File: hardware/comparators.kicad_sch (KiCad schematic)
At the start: 108 parts, among them SW7 SW_DIP_x03, U41 TLV3502AIDR, U42 TLV3502AIDR, U43 TLV3502AIDR, U44 TLV3502AIDR, U45 TLV3502AIDR, U46 TLV3502AIDR, U47 TLV3502AIDR, U48 TLV3502AIDR, U49 TLV3502AIDR, U50 TLV3502AIDR, U51 TLV3502AIDR, U52 TLV3502AIDR, U53 TXB0108PW, U54 TXB0108PW, U55 TXB0108PW

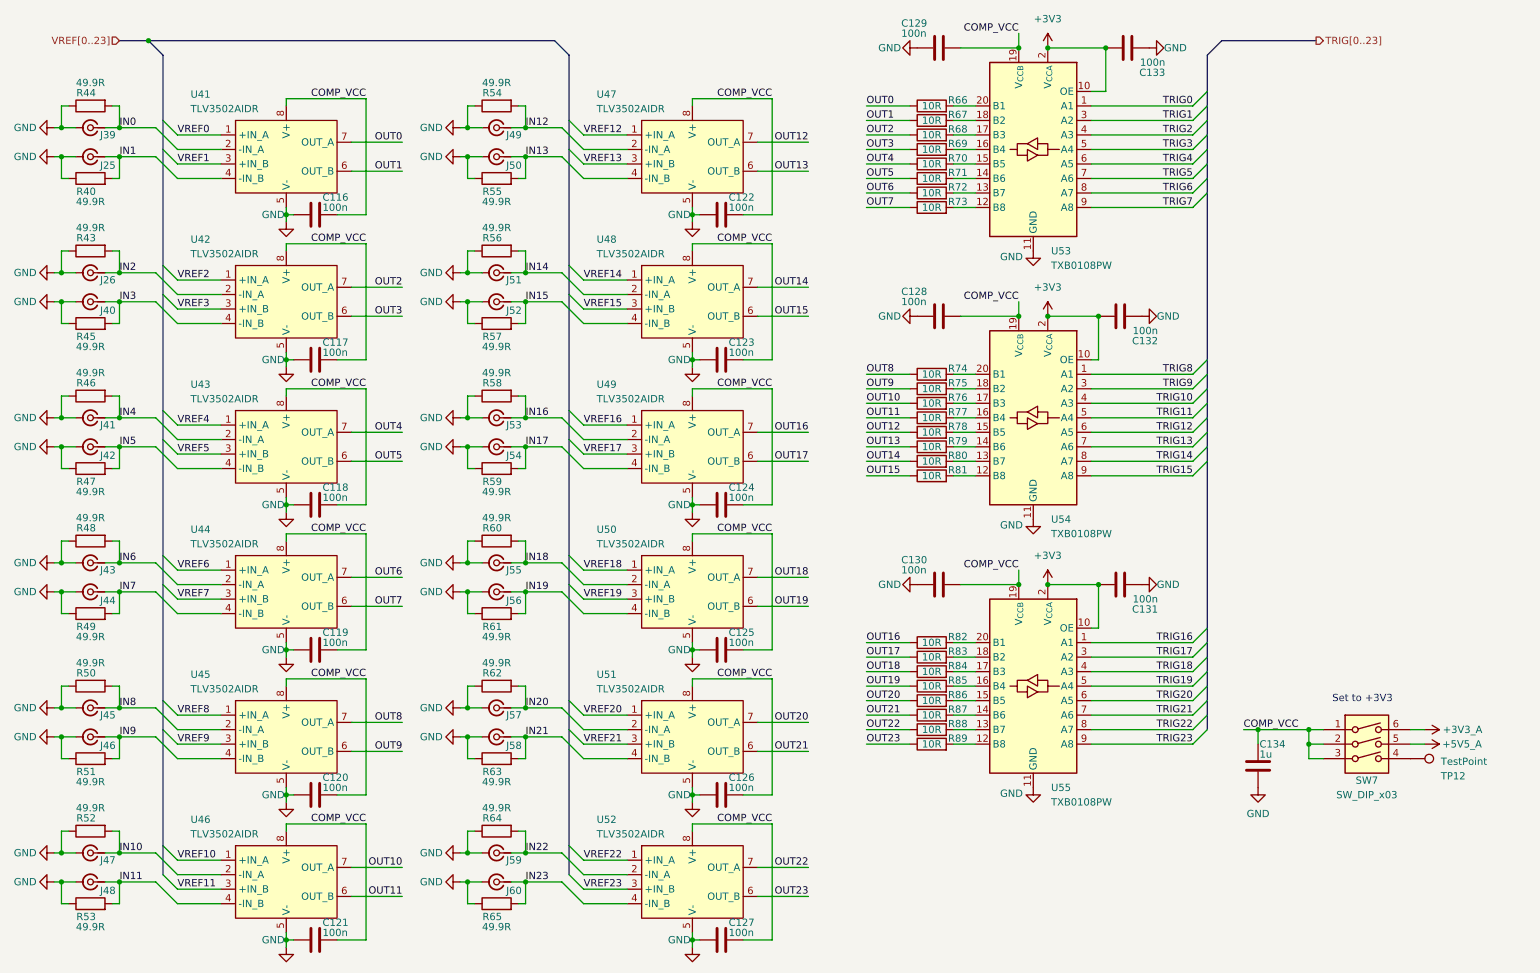
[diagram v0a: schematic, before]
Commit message: complete schematic wiring
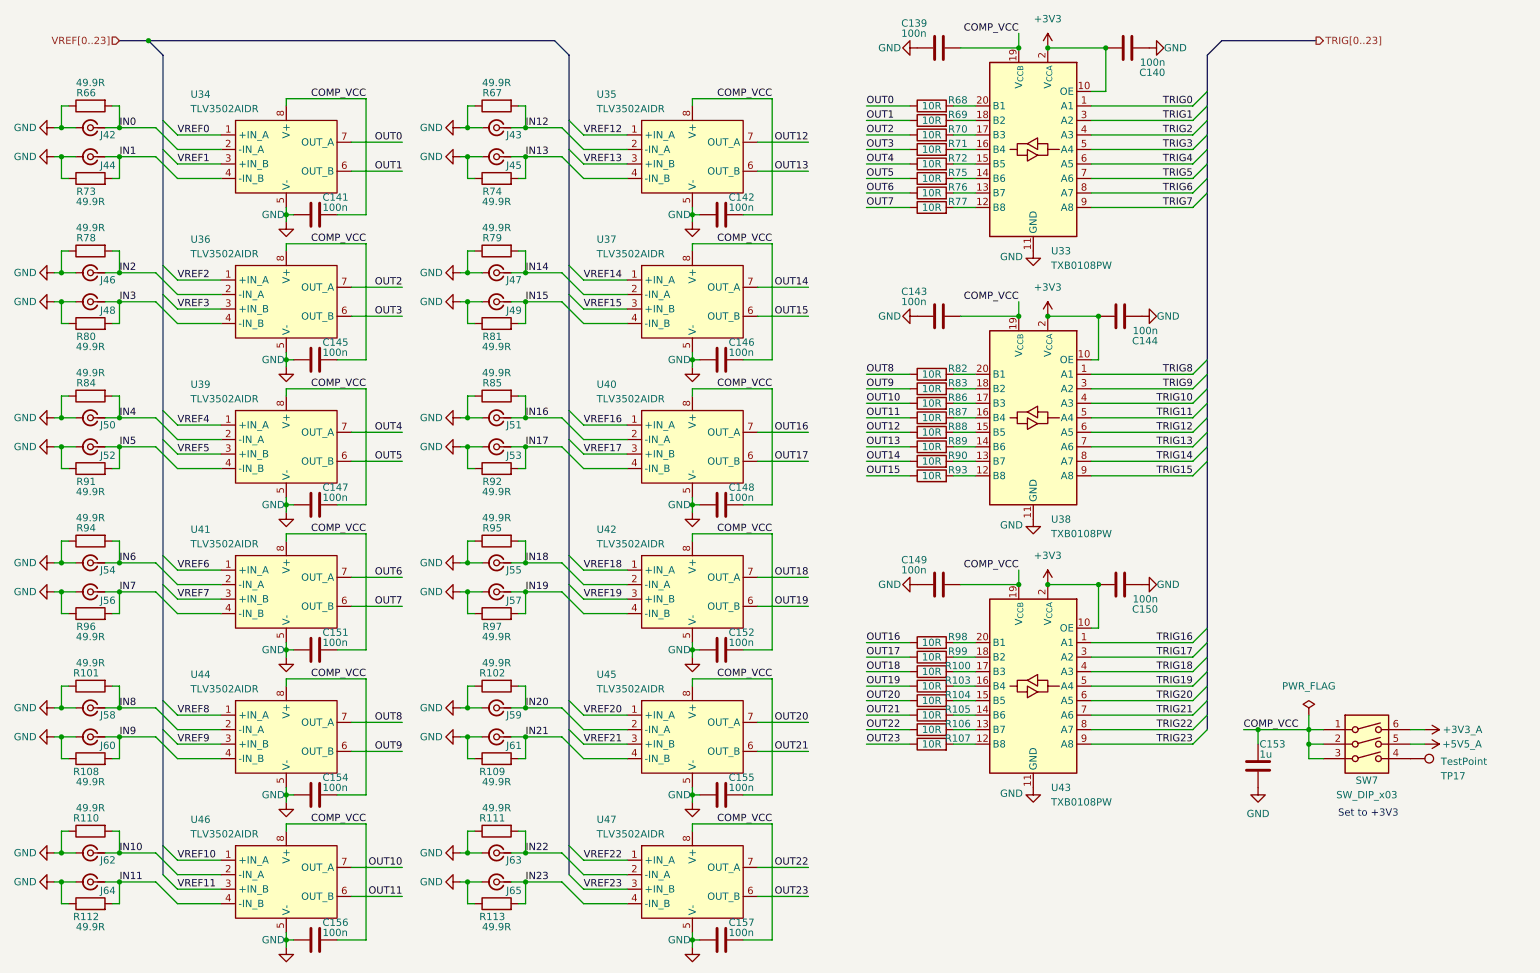
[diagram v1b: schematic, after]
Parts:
- renumbered C129 to C139, C133 to C140, C116 to C141, C122 to C142, C128 to C143, C132 to C144, C117 to C145, C123 to C146, C118 to C147, C124 to C148, C130 to C149, C131 to C150, C119 to C151, C125 to C152, C134 to C153, C120 to C154, C126 to C155, C121 to C156, C127 to C157, J39 to J42, J49 to J43, J25 to J44, J50 to J45, J26 to J46, J51 to J47, J40 to J48, J52 to J49, J41 to J50, J53 to J51, J42 to J52, J54 to J53, J43 to J54, J44 to J56, J56 to J57, J45 to J58, J57 to J59, J46 to J60, J58 to J61, J47 to J62, J59 to J63, J48 to J64, J60 to J65, R84 to R100, R50 to R101, R62 to R102, R85 to R103, R86 to R104, R87 to R105, R88 to R106, R89 to R107, R51 to R108, R63 to R109, R52 to R110, R64 to R111, R53 to R112, R65 to R113, R44 to R66, R54 to R67, R66 to R68, R67 to R69, R68 to R70, R69 to R71, R70 to R72, R40 to R73, R55 to R74, R71 to R75, R72 to R76, R73 to R77, R43 to R78, R56 to R79, R45 to R80, R57 to R81, R74 to R82, R75 to R83, R46 to R84, R58 to R85, R76 to R86, R77 to R87, R78 to R88, R79 to R89, R80 to R90, R47 to R91, R59 to R92, R81 to R93, R48 to R94, R60 to R95, R49 to R96, R61 to R97, R82 to R98, R83 to R99, TP12 to TP17, U53 to U33, U41 to U34, U47 to U35, U42 to U36, U48 to U37, U54 to U38, U43 to U39, U49 to U40, U44 to U41, U50 to U42, U55 to U43, U45 to U44, U51 to U45, U52 to U47

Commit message: update power system + add LCSC part numbers
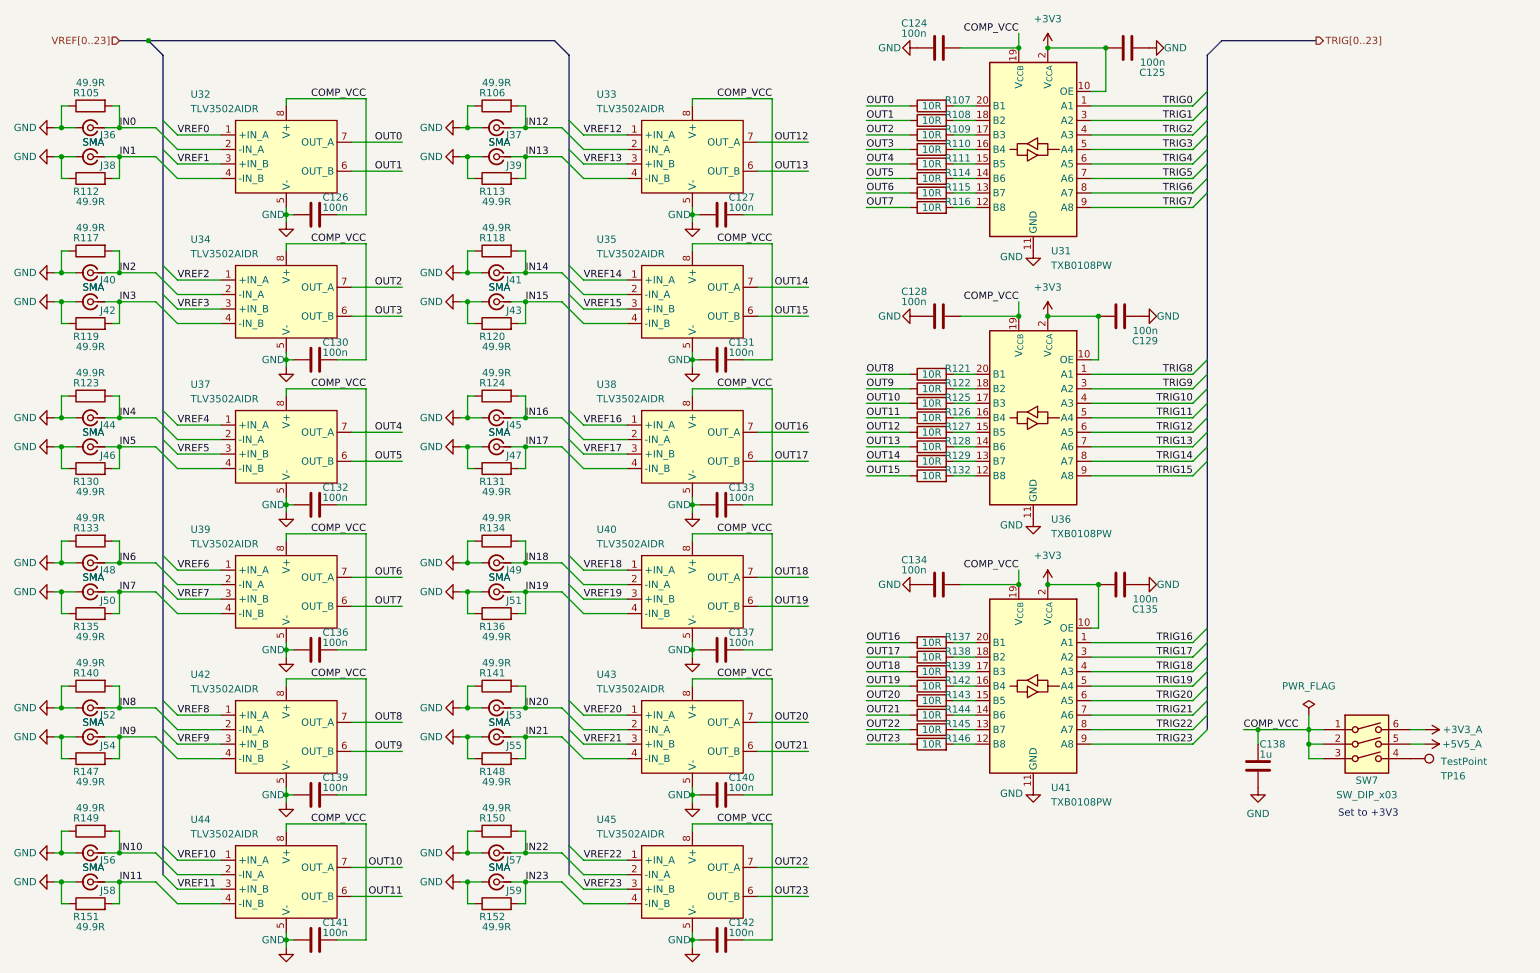
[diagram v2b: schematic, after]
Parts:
- C124: renamed from C139; footprint (none) -> Capacitor_SMD:C_0402_1005Metric; LCSC (none) -> C307331
- C125: renamed from C140; footprint (none) -> Capacitor_SMD:C_0402_1005Metric; LCSC (none) -> C307331
- C126: renamed from C141; footprint (none) -> Capacitor_SMD:C_0402_1005Metric; LCSC (none) -> C307331
- C127: renamed from C142; footprint (none) -> Capacitor_SMD:C_0402_1005Metric; LCSC (none) -> C307331
- C128: renamed from C143; footprint (none) -> Capacitor_SMD:C_0402_1005Metric; LCSC (none) -> C307331
- C129: renamed from C144; footprint (none) -> Capacitor_SMD:C_0402_1005Metric; LCSC (none) -> C307331
- C130: renamed from C145; footprint (none) -> Capacitor_SMD:C_0402_1005Metric; LCSC (none) -> C307331
- C131: renamed from C146; footprint (none) -> Capacitor_SMD:C_0402_1005Metric; LCSC (none) -> C307331
- C132: renamed from C147; footprint (none) -> Capacitor_SMD:C_0402_1005Metric; LCSC (none) -> C307331
- C133: renamed from C148; footprint (none) -> Capacitor_SMD:C_0402_1005Metric; LCSC (none) -> C307331
- C134: renamed from C149; footprint (none) -> Capacitor_SMD:C_0402_1005Metric; LCSC (none) -> C307331
- C135: renamed from C150; footprint (none) -> Capacitor_SMD:C_0402_1005Metric; LCSC (none) -> C307331
- C136: renamed from C151; footprint (none) -> Capacitor_SMD:C_0402_1005Metric; LCSC (none) -> C307331
- C137: renamed from C152; footprint (none) -> Capacitor_SMD:C_0402_1005Metric; LCSC (none) -> C307331
- C138: renamed from C153; footprint (none) -> Capacitor_SMD:C_0805_2012Metric; LCSC (none) -> C28323
- C139: renamed from C154; footprint (none) -> Capacitor_SMD:C_0402_1005Metric; LCSC (none) -> C307331
- C140: renamed from C155; footprint (none) -> Capacitor_SMD:C_0402_1005Metric; LCSC (none) -> C307331
- C141: renamed from C156; footprint (none) -> Capacitor_SMD:C_0402_1005Metric; LCSC (none) -> C307331
- C142: renamed from C157; footprint (none) -> Capacitor_SMD:C_0402_1005Metric; LCSC (none) -> C307331
- J36: renamed from J42; value ~ -> SMA; footprint (none) -> Connector_Coaxial:SMA_Amphenol_901-144_Vertical
- J37: renamed from J43; value ~ -> SMA; footprint (none) -> Connector_Coaxial:SMA_Amphenol_901-144_Vertical
- J38: renamed from J44; value ~ -> SMA; footprint (none) -> Connector_Coaxial:SMA_Amphenol_901-144_Vertical
- J39: renamed from J45; value ~ -> SMA; footprint (none) -> Connector_Coaxial:SMA_Amphenol_901-144_Vertical
- J40: renamed from J46; value ~ -> SMA; footprint (none) -> Connector_Coaxial:SMA_Amphenol_901-144_Vertical
- J41: renamed from J47; value ~ -> SMA; footprint (none) -> Connector_Coaxial:SMA_Amphenol_901-144_Vertical
- J42: renamed from J48; value ~ -> SMA; footprint (none) -> Connector_Coaxial:SMA_Amphenol_901-144_Vertical
- J43: renamed from J49; value ~ -> SMA; footprint (none) -> Connector_Coaxial:SMA_Amphenol_901-144_Vertical
- J44: renamed from J50; value ~ -> SMA; footprint (none) -> Connector_Coaxial:SMA_Amphenol_901-144_Vertical
- J45: renamed from J51; value ~ -> SMA; footprint (none) -> Connector_Coaxial:SMA_Amphenol_901-144_Vertical
- J46: renamed from J52; value ~ -> SMA; footprint (none) -> Connector_Coaxial:SMA_Amphenol_901-144_Vertical
- J47: renamed from J53; value ~ -> SMA; footprint (none) -> Connector_Coaxial:SMA_Amphenol_901-144_Vertical
- J48: renamed from J54; value ~ -> SMA; footprint (none) -> Connector_Coaxial:SMA_Amphenol_901-144_Vertical
- J49: renamed from J55; value ~ -> SMA; footprint (none) -> Connector_Coaxial:SMA_Amphenol_901-144_Vertical
- J50: renamed from J56; value ~ -> SMA; footprint (none) -> Connector_Coaxial:SMA_Amphenol_901-144_Vertical
- J51: renamed from J57; value ~ -> SMA; footprint (none) -> Connector_Coaxial:SMA_Amphenol_901-144_Vertical
- J52: renamed from J58; value ~ -> SMA; footprint (none) -> Connector_Coaxial:SMA_Amphenol_901-144_Vertical
- J53: renamed from J59; value ~ -> SMA; footprint (none) -> Connector_Coaxial:SMA_Amphenol_901-144_Vertical
- J54: renamed from J60; value ~ -> SMA; footprint (none) -> Connector_Coaxial:SMA_Amphenol_901-144_Vertical
- J55: renamed from J61; value ~ -> SMA; footprint (none) -> Connector_Coaxial:SMA_Amphenol_901-144_Vertical
- J56: renamed from J62; value ~ -> SMA; footprint (none) -> Connector_Coaxial:SMA_Amphenol_901-144_Vertical
- J57: renamed from J63; value ~ -> SMA; footprint (none) -> Connector_Coaxial:SMA_Amphenol_901-144_Vertical
- J58: renamed from J64; value ~ -> SMA; footprint (none) -> Connector_Coaxial:SMA_Amphenol_901-144_Vertical
- J59: renamed from J65; value ~ -> SMA; footprint (none) -> Connector_Coaxial:SMA_Amphenol_901-144_Vertical
- R105: renamed from R66; footprint (none) -> Resistor_SMD:R_0603_1608Metric; LCSC (none) -> C23185
- R106: renamed from R67; footprint (none) -> Resistor_SMD:R_0603_1608Metric; LCSC (none) -> C23185
- R107: renamed from R68; footprint (none) -> Resistor_SMD:R_0402_1005Metric; LCSC (none) -> C25077
- R108: renamed from R69; footprint (none) -> Resistor_SMD:R_0402_1005Metric; LCSC (none) -> C25077
- R109: renamed from R70; footprint (none) -> Resistor_SMD:R_0402_1005Metric; LCSC (none) -> C25077
- R110: renamed from R71; footprint (none) -> Resistor_SMD:R_0402_1005Metric; LCSC (none) -> C25077
- R111: renamed from R72; footprint (none) -> Resistor_SMD:R_0402_1005Metric; LCSC (none) -> C25077
- R112: renamed from R73; footprint (none) -> Resistor_SMD:R_0603_1608Metric; LCSC (none) -> C23185
- R113: renamed from R74; footprint (none) -> Resistor_SMD:R_0603_1608Metric; LCSC (none) -> C23185
- R114: renamed from R75; footprint (none) -> Resistor_SMD:R_0402_1005Metric; LCSC (none) -> C25077
- R115: renamed from R76; footprint (none) -> Resistor_SMD:R_0402_1005Metric; LCSC (none) -> C25077
- R116: renamed from R77; footprint (none) -> Resistor_SMD:R_0402_1005Metric; LCSC (none) -> C25077
- R117: renamed from R78; footprint (none) -> Resistor_SMD:R_0603_1608Metric; LCSC (none) -> C23185
- R118: renamed from R79; footprint (none) -> Resistor_SMD:R_0603_1608Metric; LCSC (none) -> C23185
- R119: renamed from R80; footprint (none) -> Resistor_SMD:R_0603_1608Metric; LCSC (none) -> C23185
- R120: renamed from R81; footprint (none) -> Resistor_SMD:R_0603_1608Metric; LCSC (none) -> C23185
- R121: renamed from R82; footprint (none) -> Resistor_SMD:R_0402_1005Metric; LCSC (none) -> C25077
- R122: renamed from R83; footprint (none) -> Resistor_SMD:R_0402_1005Metric; LCSC (none) -> C25077
- R123: renamed from R84; footprint (none) -> Resistor_SMD:R_0603_1608Metric; LCSC (none) -> C23185
- R124: renamed from R85; footprint (none) -> Resistor_SMD:R_0603_1608Metric; LCSC (none) -> C23185
- R125: renamed from R86; footprint (none) -> Resistor_SMD:R_0402_1005Metric; LCSC (none) -> C25077
- R126: renamed from R87; footprint (none) -> Resistor_SMD:R_0402_1005Metric; LCSC (none) -> C25077
- R127: renamed from R88; footprint (none) -> Resistor_SMD:R_0402_1005Metric; LCSC (none) -> C25077
- R128: renamed from R89; footprint (none) -> Resistor_SMD:R_0402_1005Metric; LCSC (none) -> C25077
- R129: renamed from R90; footprint (none) -> Resistor_SMD:R_0402_1005Metric; LCSC (none) -> C25077
- R130: renamed from R91; footprint (none) -> Resistor_SMD:R_0603_1608Metric; LCSC (none) -> C23185
- R131: renamed from R92; footprint (none) -> Resistor_SMD:R_0603_1608Metric; LCSC (none) -> C23185
- R132: renamed from R93; footprint (none) -> Resistor_SMD:R_0402_1005Metric; LCSC (none) -> C25077
- R133: renamed from R94; footprint (none) -> Resistor_SMD:R_0603_1608Metric; LCSC (none) -> C23185
- R134: renamed from R95; footprint (none) -> Resistor_SMD:R_0603_1608Metric; LCSC (none) -> C23185
- R135: renamed from R96; footprint (none) -> Resistor_SMD:R_0603_1608Metric; LCSC (none) -> C23185
- R136: renamed from R97; footprint (none) -> Resistor_SMD:R_0603_1608Metric; LCSC (none) -> C23185
- R137: renamed from R98; footprint (none) -> Resistor_SMD:R_0402_1005Metric; LCSC (none) -> C25077
- R138: renamed from R99; footprint (none) -> Resistor_SMD:R_0402_1005Metric; LCSC (none) -> C25077
- R139: renamed from R100; footprint (none) -> Resistor_SMD:R_0402_1005Metric; LCSC (none) -> C25077
- R140: renamed from R101; footprint (none) -> Resistor_SMD:R_0603_1608Metric; LCSC (none) -> C23185
- R141: renamed from R102; footprint (none) -> Resistor_SMD:R_0603_1608Metric; LCSC (none) -> C23185
- R142: renamed from R103; footprint (none) -> Resistor_SMD:R_0402_1005Metric; LCSC (none) -> C25077
- R143: renamed from R104; footprint (none) -> Resistor_SMD:R_0402_1005Metric; LCSC (none) -> C25077
- R144: renamed from R105; footprint (none) -> Resistor_SMD:R_0402_1005Metric; LCSC (none) -> C25077
- R145: renamed from R106; footprint (none) -> Resistor_SMD:R_0402_1005Metric; LCSC (none) -> C25077
- R146: renamed from R107; footprint (none) -> Resistor_SMD:R_0402_1005Metric; LCSC (none) -> C25077
- R147: renamed from R108; footprint (none) -> Resistor_SMD:R_0603_1608Metric; LCSC (none) -> C23185
- R148: renamed from R109; footprint (none) -> Resistor_SMD:R_0603_1608Metric; LCSC (none) -> C23185
- R149: renamed from R110; footprint (none) -> Resistor_SMD:R_0603_1608Metric; LCSC (none) -> C23185
- R150: renamed from R111; footprint (none) -> Resistor_SMD:R_0603_1608Metric; LCSC (none) -> C23185
- R151: renamed from R112; footprint (none) -> Resistor_SMD:R_0603_1608Metric; LCSC (none) -> C23185
- R152: renamed from R113; footprint (none) -> Resistor_SMD:R_0603_1608Metric; LCSC (none) -> C23185
- SW7: footprint (none) -> Button_Switch_SMD:SW_DIP_SPSTx03_Slide_6.7x9.18mm_W8.61mm_P2.54mm_LowProfile; LCSC (none) -> C129079
- TP16: renamed from TP17; footprint (none) -> TestPoint:TestPoint_Pad_D1.0mm
- U31: renamed from U33; LCSC (none) -> C53406
- U32: renamed from U34; footprint (none) -> Package_SO:SOIC-8_3.9x4.9mm_P1.27mm
- U33: renamed from U35; footprint (none) -> Package_SO:SOIC-8_3.9x4.9mm_P1.27mm
- U34: renamed from U36; footprint (none) -> Package_SO:SOIC-8_3.9x4.9mm_P1.27mm
- U35: renamed from U37; footprint (none) -> Package_SO:SOIC-8_3.9x4.9mm_P1.27mm
- U36: renamed from U38; LCSC (none) -> C53406
- U37: renamed from U39; footprint (none) -> Package_SO:SOIC-8_3.9x4.9mm_P1.27mm
- U38: renamed from U40; footprint (none) -> Package_SO:SOIC-8_3.9x4.9mm_P1.27mm
- U39: renamed from U41; footprint (none) -> Package_SO:SOIC-8_3.9x4.9mm_P1.27mm
- U40: renamed from U42; footprint (none) -> Package_SO:SOIC-8_3.9x4.9mm_P1.27mm
- U41: renamed from U43; LCSC (none) -> C53406
- U42: renamed from U44; footprint (none) -> Package_SO:SOIC-8_3.9x4.9mm_P1.27mm
- U43: renamed from U45; footprint (none) -> Package_SO:SOIC-8_3.9x4.9mm_P1.27mm
- U44: renamed from U46; footprint (none) -> Package_SO:SOIC-8_3.9x4.9mm_P1.27mm
- U45: renamed from U47; footprint (none) -> Package_SO:SOIC-8_3.9x4.9mm_P1.27mm

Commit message: apply manufacturing BOM
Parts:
- renumbered C124 to C128, C125 to C129, C126 to C130, C127 to C131, C128 to C132, C129 to C133, C130 to C134, C131 to C135, C132 to C136, C133 to C137, C134 to C138, C135 to C139, C136 to C140, C137 to C141, C138 to C142, C139 to C143, C140 to C144, C141 to C145, C142 to C146, J36 to J35, J37 to J36, J38 to J37, J39 to J38, J40 to J39, J41 to J40, J42 to J41, J43 to J42, J44 to J43, J45 to J44, J46 to J45, J47 to J46, J48 to J47, J49 to J48, J50 to J49, J51 to J50, J52 to J51, J53 to J52, J54 to J53, J55 to J54, J56 to J55, J57 to J56, J58 to J57, J59 to J58, R105 to R113, R106 to R114, R107 to R115, R108 to R116, R109 to R117, R110 to R118, R111 to R119, R112 to R120, R113 to R121, R114 to R122, R115 to R123, R116 to R124, R117 to R125, R118 to R126, R119 to R127, R120 to R128, R121 to R129, R122 to R130, R123 to R131, R124 to R132, R125 to R133, R126 to R134, R127 to R135, R128 to R136, R129 to R137, R130 to R138, R131 to R139, R132 to R140, R133 to R141, R134 to R142, R135 to R143, R136 to R144, R137 to R145, R138 to R146, R139 to R147, R140 to R148, R141 to R149, R142 to R150, R143 to R151, R144 to R152, R145 to R153, R146 to R154, R147 to R155, R148 to R156, R149 to R157, R150 to R158, R151 to R159, R152 to R160
